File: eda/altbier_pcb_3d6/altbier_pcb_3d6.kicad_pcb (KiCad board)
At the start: 2 copper layers, 121.2 x 140 mm, 62 parts, among them IC1 IC_CH552G, J1 USB_B_Micro, J2 Conn_01x02, SW1 SPDT_C136659, SW2 TS2306A, SW3 SW_Push_SPST_4pin

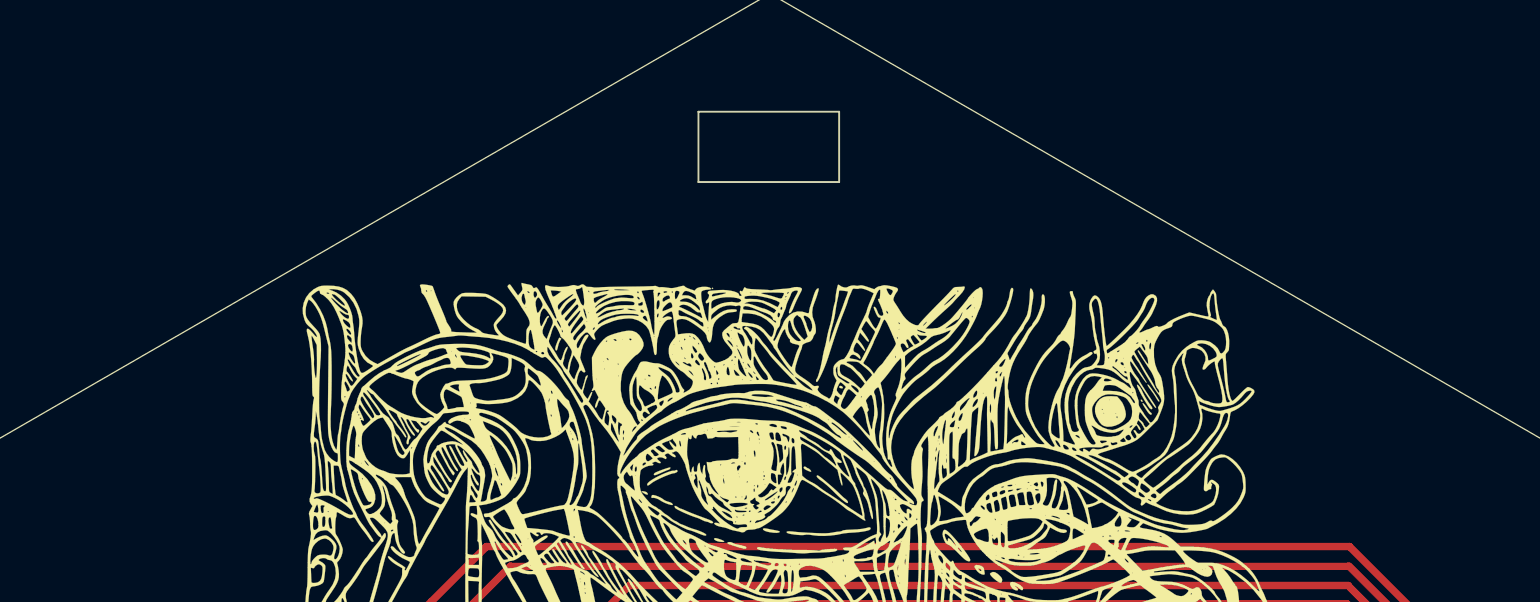
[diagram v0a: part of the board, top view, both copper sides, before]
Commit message: Updated design to allow for dual connect lanyard.
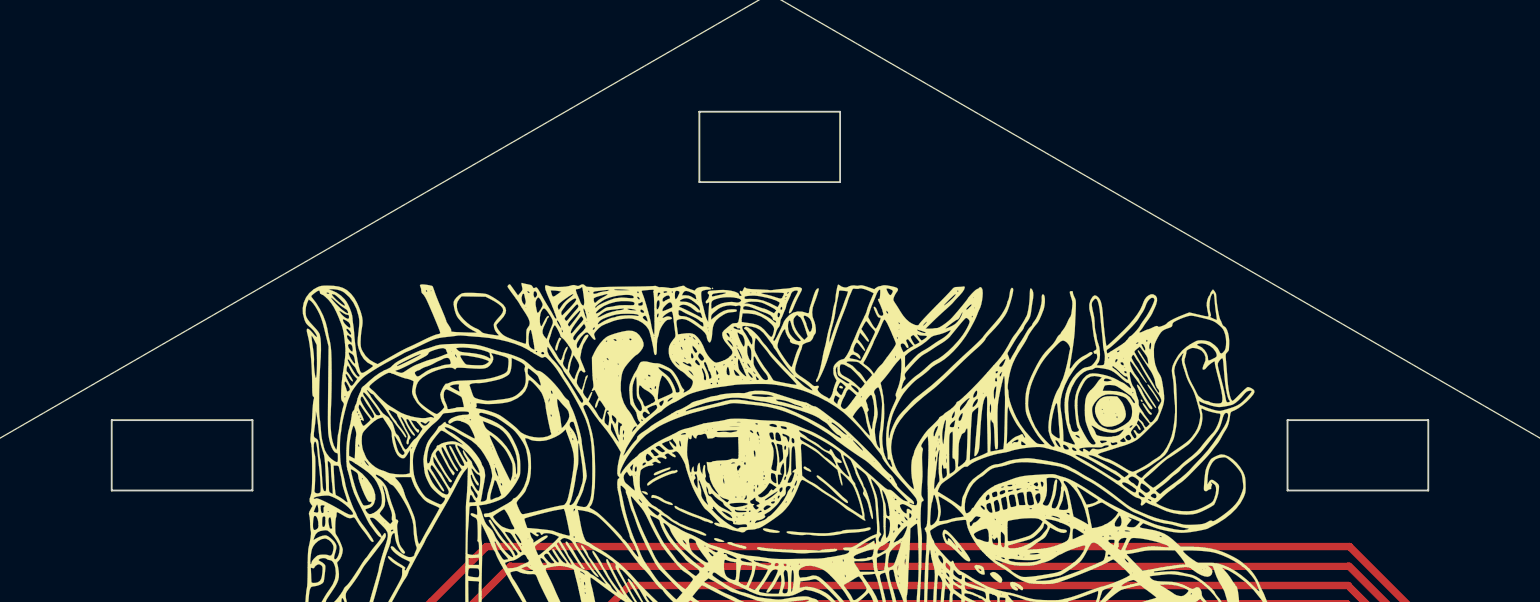
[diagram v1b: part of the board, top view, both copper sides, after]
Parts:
- D11, D12, D13, D14, D15, D16, D17: value Red -> Blue
- D21, D22, D23, D24, D25, D26, D27: value Green -> Blue
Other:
- outline, holes or cut-outs redrawn
